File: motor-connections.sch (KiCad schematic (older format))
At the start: 18 parts, among them J3 Conn_02x01, J4 Conn_01x03, J5 Conn_01x04, Q1 Q_NPN_BCE, Q2 Q_PMOS_DGS, U2 Opamp_Quad_Generic

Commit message: Fixed amplifier circuit and did some rearranging
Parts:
- removed D1: D_Zener, symbol Device:D_Zener
- removed U2: Opamp_Quad_Generic, symbol Device:Opamp_Quad_Generic
- added D1: D_Schottky_x2_Serial_AKC, symbol Device:D_Schottky_x2_Serial_AKC
- added R7: 47k, symbol Device:R
- added U3: OPA333xxDCK, symbol Amplifier_Operational:OPA333xxDCK
- C7: renamed from C5; value C -> 100n
- R6: renamed from R7; value 4.7k -> 5.23k
- R8: renamed from R?; value R -> 10k
- renumbered R6 to R10, R9 to R11, R10 to R12, R4 to R2, R5 to R3, R2 to R4, R3 to R5, R8 to R9
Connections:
- net labels added: +3V3, MOTOR_CONTROL, MOTOR_DISCONNECT, MOTOR_SENSE, ROT_CLK, ROT_DAT
- net labels removed: MOTOR_A_CONTROL, MOTOR_A_DISCONNECT, MOTOR_A_SENSE, ROT_CLK_A, ROT_DAT_A
- wire segments 54 -> 60
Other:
- note added: "Clamping"
- note added: "Continuous current: 8A\nSpike current: 15A\nShunt resistor to dissipate < 0.5W continuous\n0.5 > 64 * R\nR = 5m\nVoltage across shunt: 40mV cont. 75mV spike\nOutput voltage range: 0 - 3.3V\nGain = 3.3 / 0.075 = 44\nResistances for diff. amp: 100, 4.7k -> gain of 47\nChange in current of 0.1A -> change in output of 0.0235V"
- note added: "Normally the non-inverting input would be connected \nvia a 4.7K resistor to GND. However, you can instead \nuse any voltage source instead of GND, in which case\nthe output will be offset by that voltage. The resistor\ndivider network R7:R6 has a thevenin equivalent\ncircuit of a 0.33V source in series with a 4.7k resistor,\ngiving an offset of 0.33V. This is to account for input\nvoltage bias a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"
- note added: "RC filter - bandwidth = 1600Hz"
- moved on the sheet: C7, J3, J4, J5, Q1, Q2, R10, R11, R12, R2, R3, R4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

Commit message: Various changes
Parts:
- added D?: LED, symbol Device:LED
- added R?: R, symbol Device:R
- J4: value Conn_01x03 -> Motor
- J5: value Conn_01x04 -> Rotary_Encoder
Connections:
- net GND: now also D?.1 (K)
- net at J3.2 (Pin_2), J4.2 (Pin_2): now also R?.1
- new net: D?.2 (A), R?.2
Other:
- moved on the sheet: J8

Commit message: Various changes.
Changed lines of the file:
@@
 $Descr A4 11693 8268
 encoding utf-8
-Sheet 3 4
+Sheet 4 4
 Title ""
 Date ""
@@
 AR Path="/618F2956/619FB0A8" Ref="R23"  Part="1"
 AR Path="/618F4190/619FB0A8" Ref="R34"  Part="1"
-F 0 "R23" H 6420 4496 50  0000 L CNN
+F 0 "R34" H 6420 4496 50  0000 L CNN
 F 1 "5m" H 6420 4405 50  0000 L CNN
 F 2 "" V 6280 4450 50  0001 C CNN
@@
 AR Path="/618F2956/619FB0AE" Ref="R20"  Part="1"
 AR Path="/618F4190/619FB0AE" Ref="R31"  Part="1"
-F 0 "R20" V 4093 4350 50  0000 C CNN
+F 0 "R31" V 4093 4350 50  0000 C CNN
 F 1 "100" V 4184 4350 50  0000 C CNN
 F 2 "" V 4230 4350 50  0001 C CNN
@@
 AR Path="/618F2956/619FB0B4" Ref="R21"  Part="1"
 AR Path="/618F4190/619FB0B4" Ref="R32"  Part="1"
-F 0 "R21" V 4400 4550 50  0000 C CNN
+F 0 "R32" V 4400 4550 50  0000 C CNN
 F 1 "100" V 4500 4550 50  0000 C CNN
 F 2 "" V 4230 4550 50  0001 C CNN
@@
 AR Path="/618F2956/619FB0D5" Ref="#PWR042"  Part="1"
 AR Path="/618F4190/619FB0D5" Ref="#PWR056"  Part="1"
-F 0 "#PWR042" H 6350 4850 50  0001 C CNN
+F 0 "#PWR056" H 6350 4850 50  0001 C CNN
 F 1 "GNDPWR" H 6354 4896 50  0000 C CNN
 F 2 "" H 6350 5000 50  0001 C CNN
@@
 AR Path="/618F2956/619FB132" Ref="J6"  Part="1"
 AR Path="/618F4190/619FB132" Ref="J9"  Part="1"
-F 0 "J6" H 5500 1967 50  0000 C CNN
+F 0 "J9" H 5500 1967 50  0000 C CNN
 F 1 "Conn_02x01" H 5500 1876 50  0000 C CNN
 F 2 "" H 5450 1750 50  0001 C CNN
@@
 AR Path="/618F2956/619FB090" Ref="R22"  Part="1"
 AR Path="/618F4190/619FB090" Ref="R33"  Part="1"
-F 0 "R22" H 6280 1354 50  0000 R CNN
+F 0 "R33" H 6280 1354 50  0000 R CNN
 F 1 "330" H 6280 1445 50  0000 R CNN
 F 2 "" V 6280 1400 50  0001 C CNN
@@
 AR Path="/618F2956/619FB142" Ref="#PWR040"  Part="1"
 AR Path="/618F4190/619FB142" Ref="#PWR054"  Part="1"
-F 0 "#PWR040" H 4600 800 50  0001 C CNN
+F 0 "#PWR054" H 4600 800 50  0001 C CNN
 F 1 "+8V" H 4615 1123 50  0000 C CNN
 F 2 "" H 4600 950 50  0001 C CNN
@@
 AR Path="/618F2956/619FB13C" Ref="#PWR036"  Part="1"
 AR Path="/618F4190/619FB13C" Ref="#PWR050"  Part="1"
-F 0 "#PWR036" H 4200 800 50  0001 C CNN
+F 0 "#PWR050" H 4200 800 50  0001 C CNN
 F 1 "+8V" H 4215 1123 50  0000 C CNN
 F 2 "" H 4200 950 50  0001 C CNN
@@
 AR Path="/618F2956/619FB0E3" Ref="Q4"  Part="1"
 AR Path="/618F4190/619FB0E3" Ref="Q6"  Part="1"
-F 0 "Q4" H 4705 1496 50  0000 L CNN
+F 0 "Q6" H 4705 1496 50  0000 L CNN
 F 1 "Q_PMOS_DGS" H 4705 1405 50  0000 L CNN
 F 2 "" H 4700 1550 50  0001 C CNN
@@
 AR Path="/618F2956/619FB0DB" Ref="Q3"  Part="1"
 AR Path="/618F4190/619FB0DB" Ref="Q5"  Part="1"
-F 0 "Q3" H 4291 1796 50  0000 L CNN
+F 0 "Q5" H 4291 1796 50  0000 L CNN
 F 1 "Q_NPN_BCE" H 3750 1550 50  0000 L CNN
 F 2 "" H 4300 1850 50  0001 C CNN
@@
 AR Path="/618F2956/619FB09C" Ref="R15"  Part="1"
 AR Path="/618F4190/619FB09C" Ref="R26"  Part="1"
-F 0 "R15" V 3443 1750 50  0000 C CNN
+F 0 "R26" V 3443 1750 50  0000 C CNN
 F 1 "10k" V 3534 1750 50  0000 C CNN
 F 2 "" V 3580 1750 50  0001 C CNN
@@
 AR Path="/618F2956/619FB096" Ref="R16"  Part="1"
 AR Path="/618F4190/619FB096" Ref="R27"  Part="1"
-F 0 "R16" H 4270 1246 50  0000 L CNN
+F 0 "R27" H 4270 1246 50  0000 L CNN
 F 1 "10k" H 4270 1155 50  0000 L CNN
 F 2 "" V 4130 1200 50  0001 C CNN
@@
 AR Path="/618F2956/619DF215" Ref="R19"  Part="1"
 AR Path="/618F4190/619DF215" Ref="R30"  Part="1"
-F 0 "R19" H 4670 2046 50  0000 L CNN
+F 0 "R30" H 4670 2046 50  0000 L CNN
 F 1 "10k" H 4670 1955 50  0000 L CNN
 F 2 "" V 4530 2000 50  0001 C CNN
@@
 AR Path="/618F2956/619DF869" Ref="#PWR041"  Part="1"
 AR Path="/618F4190/619DF869" Ref="#PWR055"  Part="1"
-F 0 "#PWR041" H 4600 1950 50  0001 C CNN
+F 0 "#PWR055" H 4600 1950 50  0001 C CNN
 F 1 "GND" H 4605 2027 50  0000 C CNN
 F 2 "" H 4600 2200 50  0001 C CNN
@@
 AR Path="/618F2956/619FB0A2" Ref="#PWR037"  Part="1"
 AR Path="/618F4190/619FB0A2" Ref="#PWR051"  Part="1"
-F 0 "#PWR037" H 4200 1950 50  0001 C CNN
+F 0 "#PWR051" H 4200 1950 50  0001 C CNN
 F 1 "GND" H 4205 2027 50  0000 C CNN
 F 2 "" H 4200 2200 50  0001 C CNN
@@
 AR Path="/618F2956/6194C7CE" Ref="#PWR033"  Part="1"
 AR Path="/618F4190/6194C7CE" Ref="#PWR047"  Part="1"
-F 0 "#PWR033" H 1900 4800 50  0001 C CNN
+F 0 "#PWR047" H 1900 4800 50  0001 C CNN
 F 1 "GND" H 1905 4877 50  0000 C CNN
 F 2 "" H 1900 5050 50  0001 C CNN
@@
 AR Path="/618F2956/6194440F" Ref="#PWR032"  Part="1"
 AR Path="/618F4190/6194440F" Ref="#PWR046"  Part="1"
-F 0 "#PWR032" H 1500 4000 50  0001 C CNN
+F 0 "#PWR046" H 1500 4000 50  0001 C CNN
 F 1 "GND" H 1650 4200 50  0000 C CNN
 F 2 "" H 1500 4250 50  0001 C CNN
@@
 AR Path="/618F2956/6194282B" Ref="#PWR031"  Part="1"
 AR Path="/618F4190/6194282B" Ref="#PWR045"  Part="1"
-F 0 "#PWR031" H 1500 3350 50  0001 C CNN
+F 0 "#PWR045" H 1500 3350 50  0001 C CNN
 F 1 "+3V3" H 1515 3673 50  0000 C CNN
 F 2 "" H 1500 3500 50  0001 C CNN
@@
 AR Path="/618F2956/6193E482" Ref="D2"  Part="1"
 AR Path="/618F4190/6193E482" Ref="D3"  Part="1"
-F 0 "D2" V 1546 3979 50  0000 L CNN
+F 0 "D3" V 1546 3979 50  0000 L CNN
 F 1 "D_Schottky_x2_Serial_AKC" V 1750 2900 50  0000 L CNN
 F 2 "" H 1500 3900 50  0001 C CNN
@@
 AR Path="/618F2956/618E8E98" Ref="#PWR039"  Part="1"
 AR Path="/618F4190/618E8E98" Ref="#PWR053"  Part="1"
-F 0 "#PWR039" H 3650 3750 50  0001 C CNN
+F 0 "#PWR053" H 3650 3750 50  0001 C CNN
 F 1 "+3V3" H 3665 4073 50  0000 C CNN
 F 2 "" H 3650 3900 50  0001 C CNN
@@
 AR Path="/618F2956/618C8A82" Ref="R18"  Part="1"
 AR Path="/618F4190/618C8A82" Ref="R29"  Part="1"
-F 0 "R18" H 3720 4146 50  0000 L CNN
+F 0 "R29" H 3720 4146 50  0000 L CNN
 F 1 "47k" H 3720 4055 50  0000 L CNN
 F 2 "" V 3580 4100 50  0001 C CNN
@@
 AR Path="/618F2956/619085BE" Ref="#PWR034"  Part="1"
 AR Path="/618F4190/619085BE" Ref="#PWR048"  Part="1"
-F 0 "#PWR034" H 2850 3800 50  0001 C CNN
+F 0 "#PWR048" H 2850 3800 50  0001 C CNN
 F 1 "+3V3" H 2865 4123 50  0000 C CNN
 F 2 "" H 2850 3950 50  0001 C CNN
@@
 AR Path="/618F2956/619FB10D" Ref="R17"  Part="1"
 AR Path="/618F4190/619FB10D" Ref="R28"  Part="1"
-F 0 "R17" H 3670 4846 50  0000 L CNN
+F 0 "R28" H 3670 4846 50  0000 L CNN
 F 1 "5.23k" H 3670 4755 50  0000 L CNN
 F 2 "" V 3530 4800 50  0001 C CNN
@@
 AR Path="/618F2956/618FC0C8" Ref="#PWR035"  Part="1"
 AR Path="/618F4190/618FC0C8" Ref="#PWR049"  Part="1"
-F 0 "#PWR035" H 2850 4800 50  0001 C CNN
+F 0 "#PWR049" H 2850 4800 50  0001 C CNN
 F 1 "GND" H 2855 4877 50  0000 C CNN
 F 2 "" H 2850 5050 50  0001 C CNN
@@
 AR Path="/618F2956/618B23D8" Ref="U4"  Part="1"
 AR Path="/618F4190/618B23D8" Ref="U5"  Part="1"
-F 0 "U4" H 2900 4750 50  0000 C CNN
+F 0 "U5" H 2900 4750 50  0000 C CNN
 F 1 "OPA333xxDCK" H 3000 4650 50  0000 C CNN
 F 2 "" H 2750 4450 50  0001 L CNN
@@
 AR Path="/618F2956/619FB116" Ref="#PWR038"  Part="1"
 AR Path="/618F4190/619FB116" Ref="#PWR052"  Part="1"
-F 0 "#PWR038" H 3600 4800 50  0001 C CNN
+F 0 "#PWR052" H 3600 4800 50  0001 C CNN
 F 1 "GND" H 3605 4877 50  0000 C CNN
 F 2 "" H 3600 5050 50  0001 C CNN
@@
 AR Path="/618F2956/619FB0EE" Ref="R14"  Part="1"
 AR Path="/618F4190/619FB0EE" Ref="R25"  Part="1"
-F 0 "R14" V 2393 4800 50  0000 C CNN
+F 0 "R25" V 2393 4800 50  0000 C CNN
 F 1 "4.7k" V 2484 4800 50  0000 C CNN
 F 2 "" V 2530 4800 50  0001 C CNN
@@
 AR Path="/618F2956/619FB0CF" Ref="R13"  Part="1"
 AR Path="/618F4190/619FB0CF" Ref="R24"  Part="1"
-F 0 "R13" V 1943 4450 50  0000 C CNN
+F 0 "R24" V 1943 4450 50  0000 C CNN
 F 1 "1k" V 2034 4450 50  0000 C CNN
 F 2 "" V 2080 4450 50  0001 C CNN
@@
 AR Path="/618F2956/619FB0BA" Ref="C8"  Part="1"
 AR Path="/618F4190/619FB0BA" Ref="C9"  Part="1"
-F 0 "C8" H 2015 4746 50  0000 L CNN
+F 0 "C9" H 2015 4746 50  0000 L CNN
 F 1 "100n" H 2015 4655 50  0000 L CNN
 F 2 "" H 1938 4550 50  0001 C CNN
@@
 AR Path="/618F2956/61A09167" Ref="#PWR044"  Part="1"
 AR Path="/618F4190/61A09167" Ref="#PWR058"  Part="1"
-F 0 "#PWR044" H 9000 2700 50  0001 C CNN
+F 0 "#PWR058" H 9000 2700 50  0001 C CNN
 F 1 "GND" H 9005 2777 50  0000 C CNN
 F 2 "" H 9000 2950 50  0001 C CNN
@@
 AR Path="/618F2956/61A09161" Ref="#PWR043"  Part="1"
 AR Path="/618F4190/61A09161" Ref="#PWR057"  Part="1"
-F 0 "#PWR043" H 9000 2150 50  0001 C CNN
+F 0 "#PWR057" H 9000 2150 50  0001 C CNN
 F 1 "+8V" H 9015 2473 50  0000 C CNN
 F 2 "" H 9000 2300 50  0001 C CNN
@@
 AR Path="/618F2956/6194BEE4" Ref="D?"  Part="1"
 AR Path="/619DAA4C/6194BEE4" Ref="D?"  Part="1"
+AR Path="/618F4190/6194BEE4" Ref="D?"  Part="1"
 F 0 "D?" V 5889 2332 50  0000 R CNN
 F 1 "LED" V 5798 2332 50  0000 R CNN
@@
 AR Path="/618F2956/6194BEEA" Ref="#PWR?"  Part="1"
 AR Path="/619DAA4C/6194BEEA" Ref="#PWR?"  Part="1"
+AR Path="/618F4190/6194BEEA" Ref="#PWR?"  Part="1"
 F 0 "#PWR?" H 5850 2450 50  0001 C CNN
 F 1 "GND" H 5855 2527 50  0000 C CNN
@@
 AR Path="/618F2956/6194BEF0" Ref="R?"  Part="1"
 AR Path="/619DAA4C/6194BEF0" Ref="R?"  Part="1"
+AR Path="/618F4190/6194BEF0" Ref="R?"  Part="1"
 F 0 "R?" H 5920 2096 50  0000 L CNN
 F 1 "R" H 5920 2005 50  0000 L CNN
@@
 AR Path="/618F2956/619FB08A" Ref="J7"  Part="1"
 AR Path="/618F4190/619FB08A" Ref="J10"  Part="1"
-F 0 "J7" H 6730 1792 50  0000 L CNN
+F 0 "J10" H 6730 1792 50  0000 L CNN
 F 1 "Motor" H 6730 1701 50  0000 L CNN
 F 2 "" H 6650 1750 50  0001 C CNN
@@
 AR Path="/618F2956/61A09153" Ref="J8"  Part="1"
 AR Path="/618F4190/61A09153" Ref="J11"  Part="1"
-F 0 "J8" H 9730 2592 50  0000 L CNN
+F 0 "J11" H 9730 2592 50  0000 L CNN
 F 1 "Rotary_Encoder" H 9730 2501 50  0000 L CNN
 F 2 "" H 9650 2600 50  0001 C CNN

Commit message: Assigned footprints
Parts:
- C7: footprint (none) -> Capacitor_SMD:C_0603_1608Metric_Pad1.05x0.95mm_HandSolder
- D10: renamed from D?; footprint (none) -> LED_SMD:LED_0603_1608Metric_Pad1.05x0.95mm_HandSolder
- R10, R11, R2, R3, R4, R5, R6, R7, R8, R9: footprint (none) -> Resistor_SMD:R_0603_1608Metric_Pad1.05x0.95mm_HandSolder
- R43: renamed from R?; footprint (none) -> Resistor_SMD:R_0603_1608Metric_Pad1.05x0.95mm_HandSolder

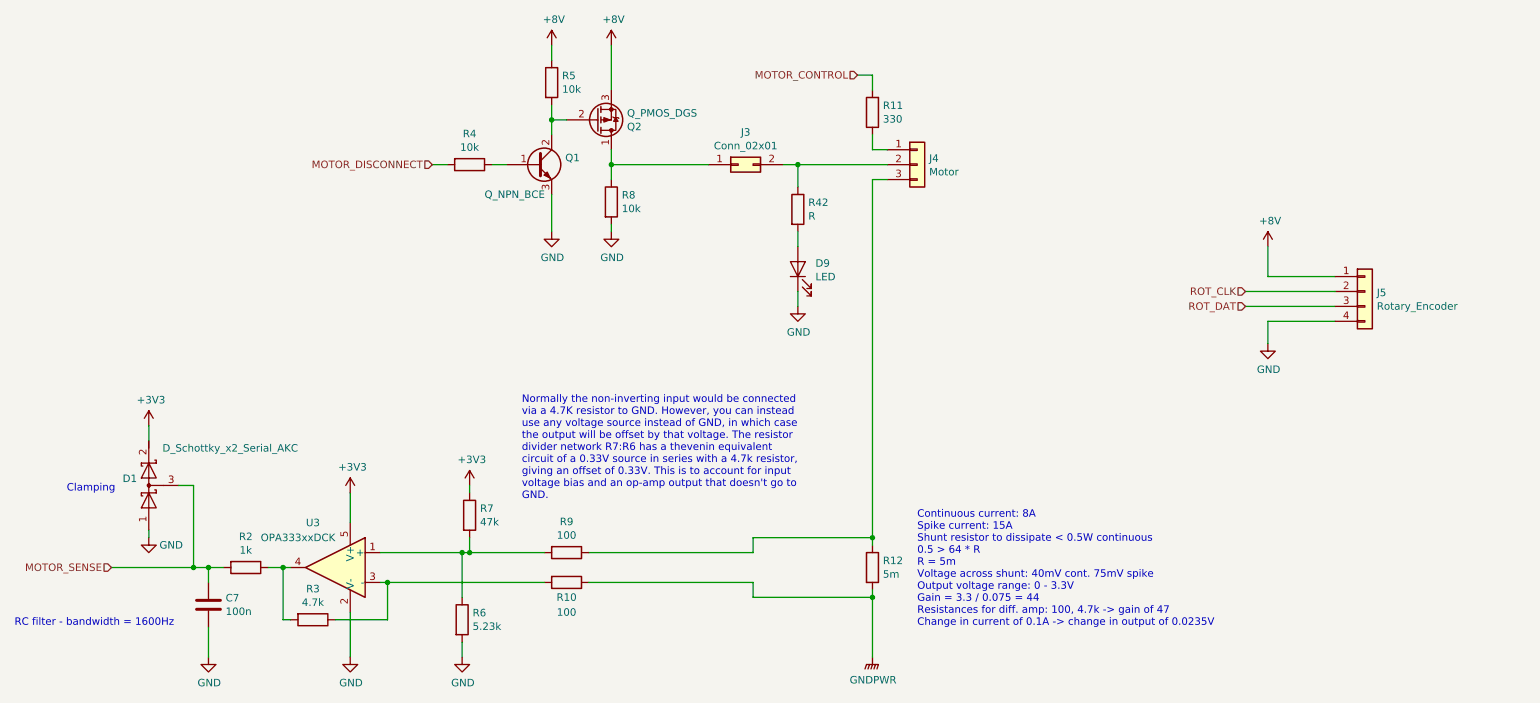
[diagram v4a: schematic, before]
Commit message: Assigned remaining footprints
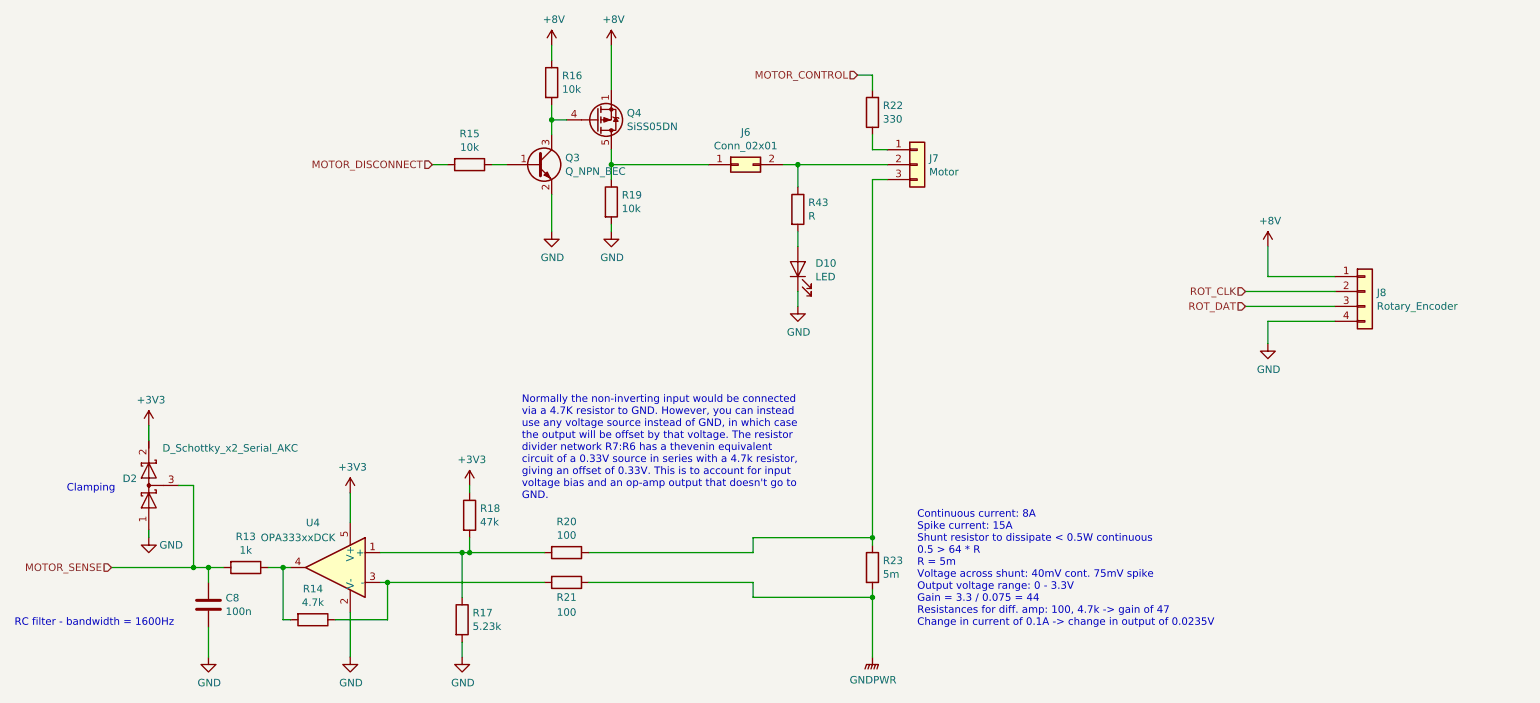
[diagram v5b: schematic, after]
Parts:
- removed Q1: Q_NPN_BCE, symbol Device:Q_NPN_BCE
- removed Q2: Q_PMOS_DGS, symbol Device:Q_PMOS_DGS
- added Q1: Q_NPN_BEC, Package_TO_SOT_SMD:SOT-23, symbol Device:Q_NPN_BEC
- added Q2: SiSS05DN, Package_SO:Vishay_PowerPAK_1212-8_Single, symbol Transistor_FET:SiS443DN
- D1: footprint (none) -> Package_TO_SOT_SMD:SOT-323_SC-70
- J3: footprint (none) -> Connector_PinHeader_2.54mm:PinHeader_1x02_P2.54mm_Vertical
- J4: footprint (none) -> Connector_PinHeader_2.54mm:PinHeader_1x03_P2.54mm_Vertical
- R12: footprint (none) -> Resistor_SMD:R_2512_6332Metric
- U3: footprint (none) -> Package_TO_SOT_SMD:SOT-353_SC-70-5_Handsoldering
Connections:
- net +8V: now also Q2.1 (S), Q2.2 (S), Q2.3 (S)
- net GND: now also Q1.2 (E)
- net at J3.1 (Pin_1), R8.1: now also Q2.5 (D)
- net at R5.2: now also Q1.3 (C), Q2.4 (G)
- net at R4.1: now also Q1.1 (B)

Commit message: Started workin on PCB layout. A bit faulty...
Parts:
- J5: footprint (none) -> Connector_PinHeader_2.54mm:PinHeader_1x04_P2.54mm_Vertical
